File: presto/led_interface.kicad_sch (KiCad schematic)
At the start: 9 parts, among them J701 LED Connector

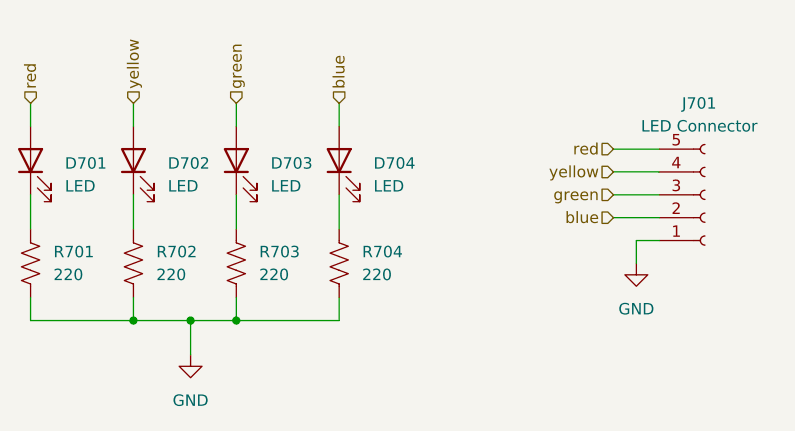
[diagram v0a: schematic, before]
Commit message: added connector for neopixel and fixed autonomy switch layout
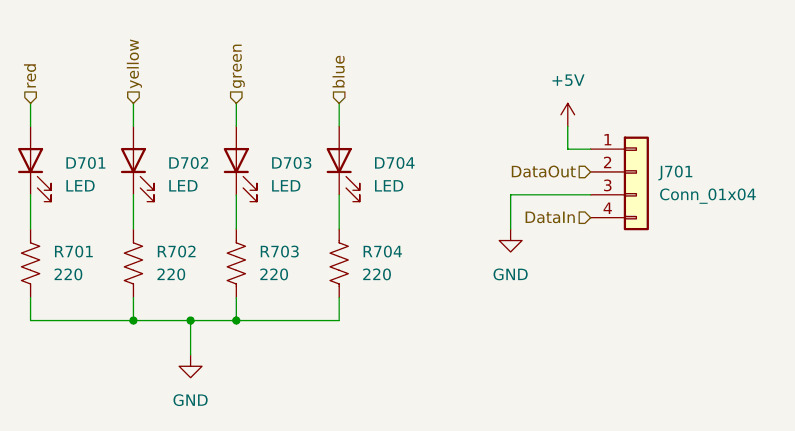
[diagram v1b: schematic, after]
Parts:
- removed J701: LED Connector, Connector_PinSocket_2.54mm:PinSocket_1x05_P2.54mm_Horizontal, symbol Connector:Conn_01x05_Socket
- added J701: Conn_01x04, Connector_JST:JST_XH_B4B-XH-A_1x04_P2.50mm_Vertical, symbol Connector_Generic:Conn_01x04
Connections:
- net GND: now also J701.3 (Pin_3)
- new net +5V: J701.1 (Pin_1)
- new net DataIn: J701.4 (Pin_4)
- new net DataOut: J701.2 (Pin_2)
